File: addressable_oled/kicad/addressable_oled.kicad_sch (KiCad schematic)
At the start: 19 parts, among them J1 Conn_01x05_Pin, J2 Conn_01x03_Socket, U1 SLG46826G, U2 OLED-128O064D

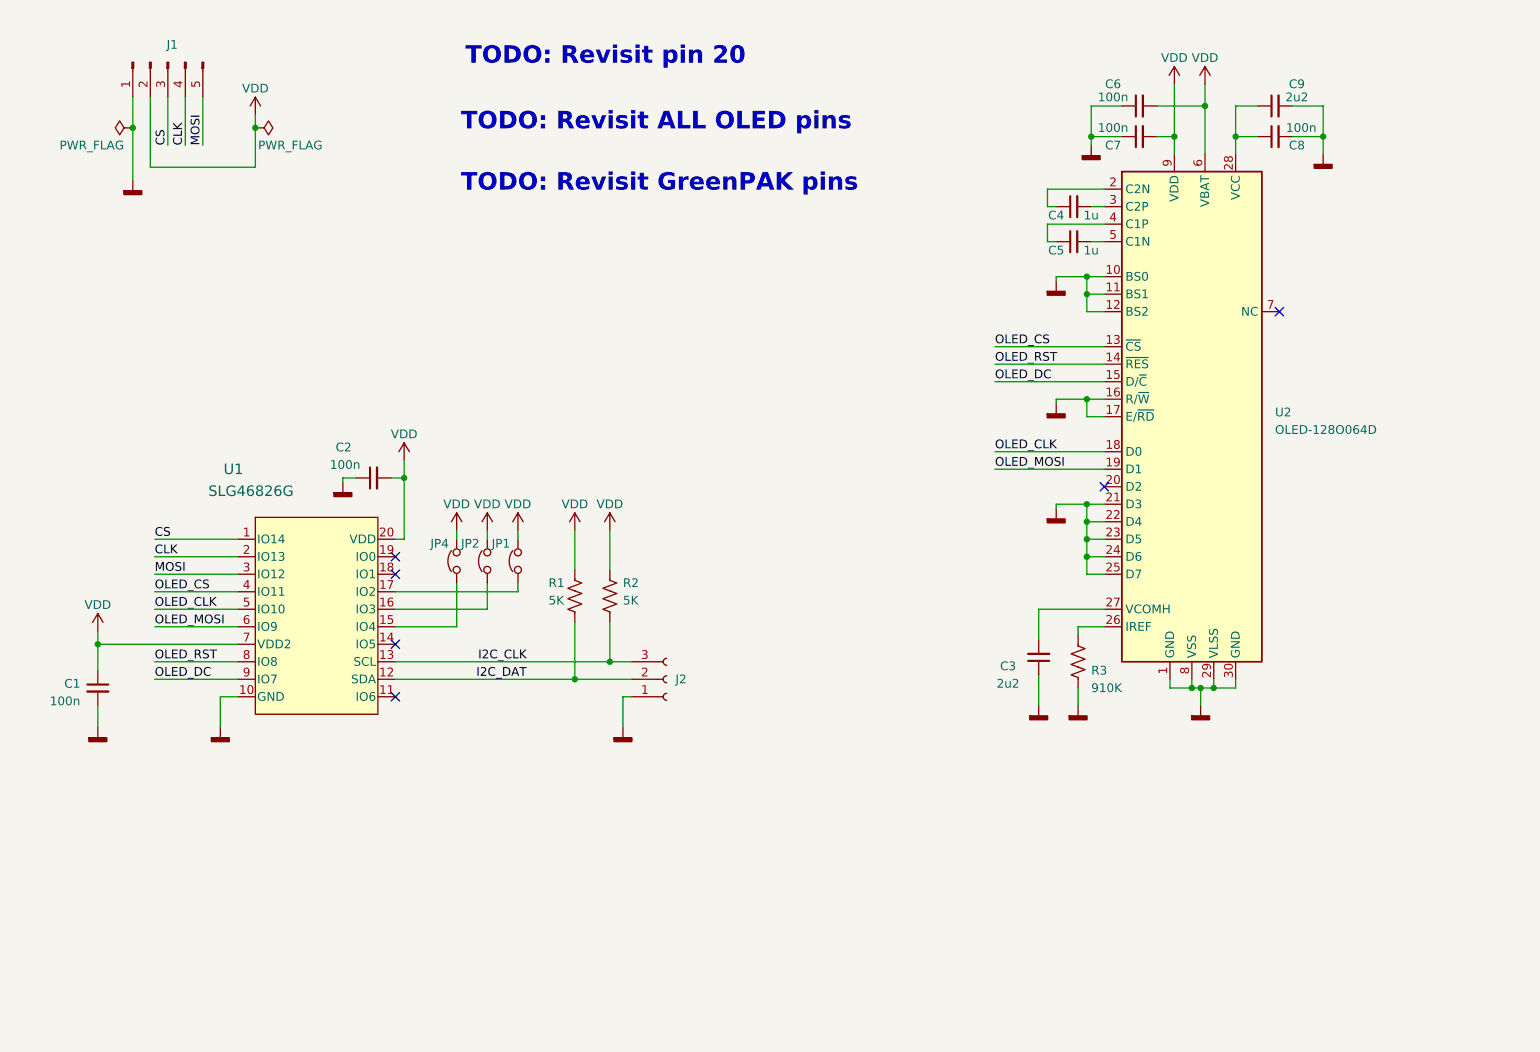
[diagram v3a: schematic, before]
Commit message: Schematic and layout in progress. Added GreenPAK pullup pins.
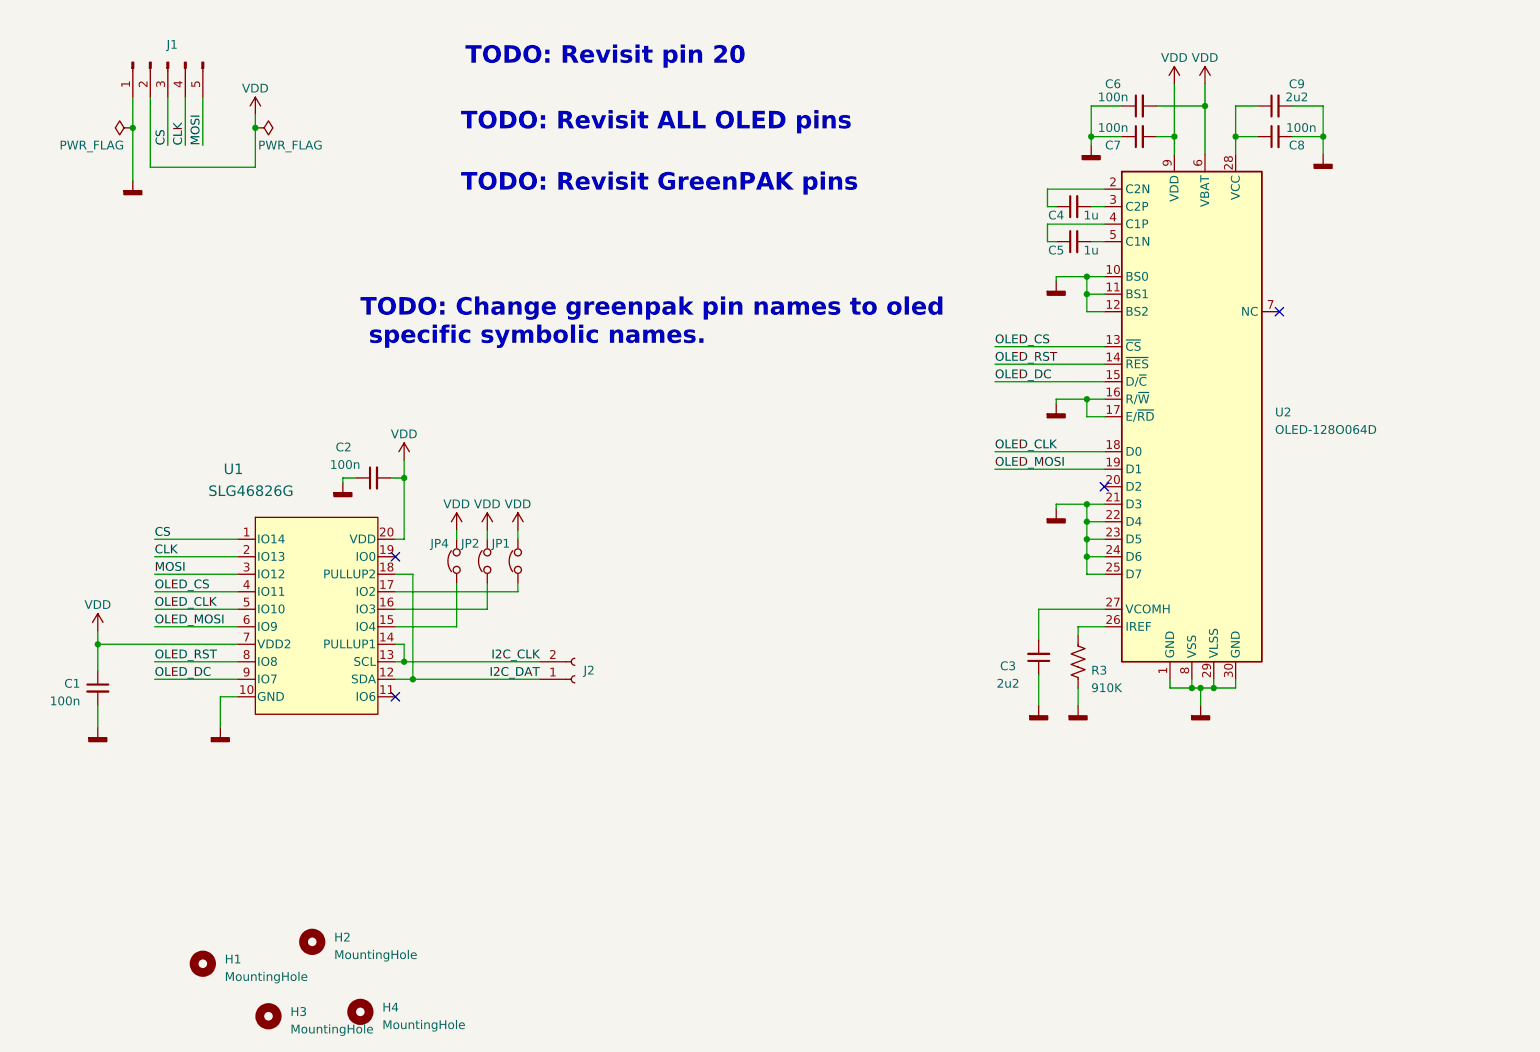
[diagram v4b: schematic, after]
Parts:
- removed R1, R2: 5K, Resistor_SMD:R_0603_1608Metric, symbol Device:R_US
- added H1, H2, H3, H4: MountingHole, symbol Mechanical:MountingHole
- J2: footprint Connector_PinHeader_2.54mm:PinHeader_1x03_P2.54mm_Vertical -> Connector_PinHeader_2.54mm:PinHeader_1x02_P2.54mm_Vertical; symbol Connector:Conn_01x03_Socket -> Connector:Conn_01x02_Socket
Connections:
- net GND: no longer J2.1 (Pin_1)
- net I2C_CLK: now also J2.2 (Pin_2), U1.14 (PULLUP1); no longer J2.3 (Pin_3)
- net I2C_DAT: now also J2.1 (Pin_1), U1.18 (PULLUP2); no longer J2.2 (Pin_2)
- no-connect marks 6 -> 4
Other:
- note added: "TODO: Change greenpak pin names to oled specific symbolic names."

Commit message: More progress with the layout.
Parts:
- C1, C2, C3, C4, C5, C6, C7, C8, C9: footprint Capacitor_SMD:C_0603_1608Metric -> addressable_oled:C_0603_1608Metric
- H1, H2, H3, H4: footprint (none) -> addressable_oled:MountingHole
- J1: footprint Connector_PinHeader_2.54mm:PinHeader_1x05_P2.54mm_Vertical -> addressable_oled:PinHeader_1x05_P2.54mm_Vertical
- J2: footprint Connector_PinHeader_2.54mm:PinHeader_1x02_P2.54mm_Vertical -> addressable_oled:PinHeader_1x04_P2.54mm_Vertical; symbol Connector:Conn_01x02_Socket -> Connector:Conn_01x04_Socket
- JP1, JP2, JP4: footprint Jumper:SolderJumper-2_P1.3mm_Open_Pad1.0x1.5mm -> addressable_oled:SolderJumper-2_P1.3mm_Open_Pad1.0x1.5mm
- R3: footprint Resistor_SMD:R_0603_1608Metric -> addressable_oled:R_0603_1608Metric
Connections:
- net GND: now also J2.1 (Pin_1)
- net I2C_CLK: now also J2.4 (Pin_4); no longer J2.2 (Pin_2)
- net I2C_DAT: now also J2.3 (Pin_3); no longer J2.1 (Pin_1)
- net VDD: now also J2.2 (Pin_2)
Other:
- note added: "PROG"
- moved on the sheet: H1, H2, H3, H4

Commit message: Switched from kicad 7.0.1-0 to 7.0.10.
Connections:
- net CLK: now also J1.3 (Pin_3); no longer J1.4 (Pin_4)
- net CS: now also J1.5 (Pin_5); no longer J1.3 (Pin_3)
- net MOSI: now also J1.4 (Pin_4); no longer J1.5 (Pin_5)
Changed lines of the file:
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@@
     (effects (font (size 2.54 2.54) (thickness 0.508) bold (color 255 0 0 1)) (justify left bottom))
   )
-  (label "CLK" (at 61.595 63.5 90) (fields_autoplaced)
+  (label "CLK" (at 59.055 63.5 90) (fields_autoplaced)
     (effects (font (size 1.27 1.27)) (justify left bottom))
   )
@@
     (effects (font (size 1.27 1.27)) (justify left bottom))
   )
-  (label "MOSI" (at 64.135 63.5 90) (fields_autoplaced)
+  (label "MOSI" (at 61.595 63.5 90) (fields_autoplaced)
     (effects (font (size 1.27 1.27)) (justify left bottom))
   )
@@
     (effects (font (size 1.27 1.27)) (justify left bottom))
   )
-  (label "CS" (at 59.055 63.5 90) (fields_autoplaced)
+  (label "CS" (at 64.135 63.5 90) (fields_autoplaced)
     (effects (font (size 1.27 1.27)) (justify left bottom))
   )

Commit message: Final cleanup.
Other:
- note added: "I2C GreenPAK PROGRAMMING"
- note added: "OLED DISPLAY PANEL"
- note added: "SPI ADDRESS DECODER"
- note added: "SPI BUS"
- note added: "SSD1306 1.3" OLED PANEL"
- note removed: "PROG"
- note removed: "TODO: Change greenpak pin names to oled specific symbolic names."
- note removed: "TODO: Revisit ALL OLED pins"
- note removed: "TODO: Revisit GreenPAK pins"
- note removed: "TODO: Revisit pin 20"
- title: (none) -> ADDRESSABLE SPI OLED
- moved on the sheet: C1, C2, C3, C4, C5, C6, C7, C8, C9, H1, H2, H3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
